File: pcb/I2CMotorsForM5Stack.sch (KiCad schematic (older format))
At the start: 25 parts, among them J1 FFC_connector, J2 2x15socket, J3 Conn_01x06, J4 Conn_01x06, U1 TB6612FNG, U2 ATmega328PB-MU

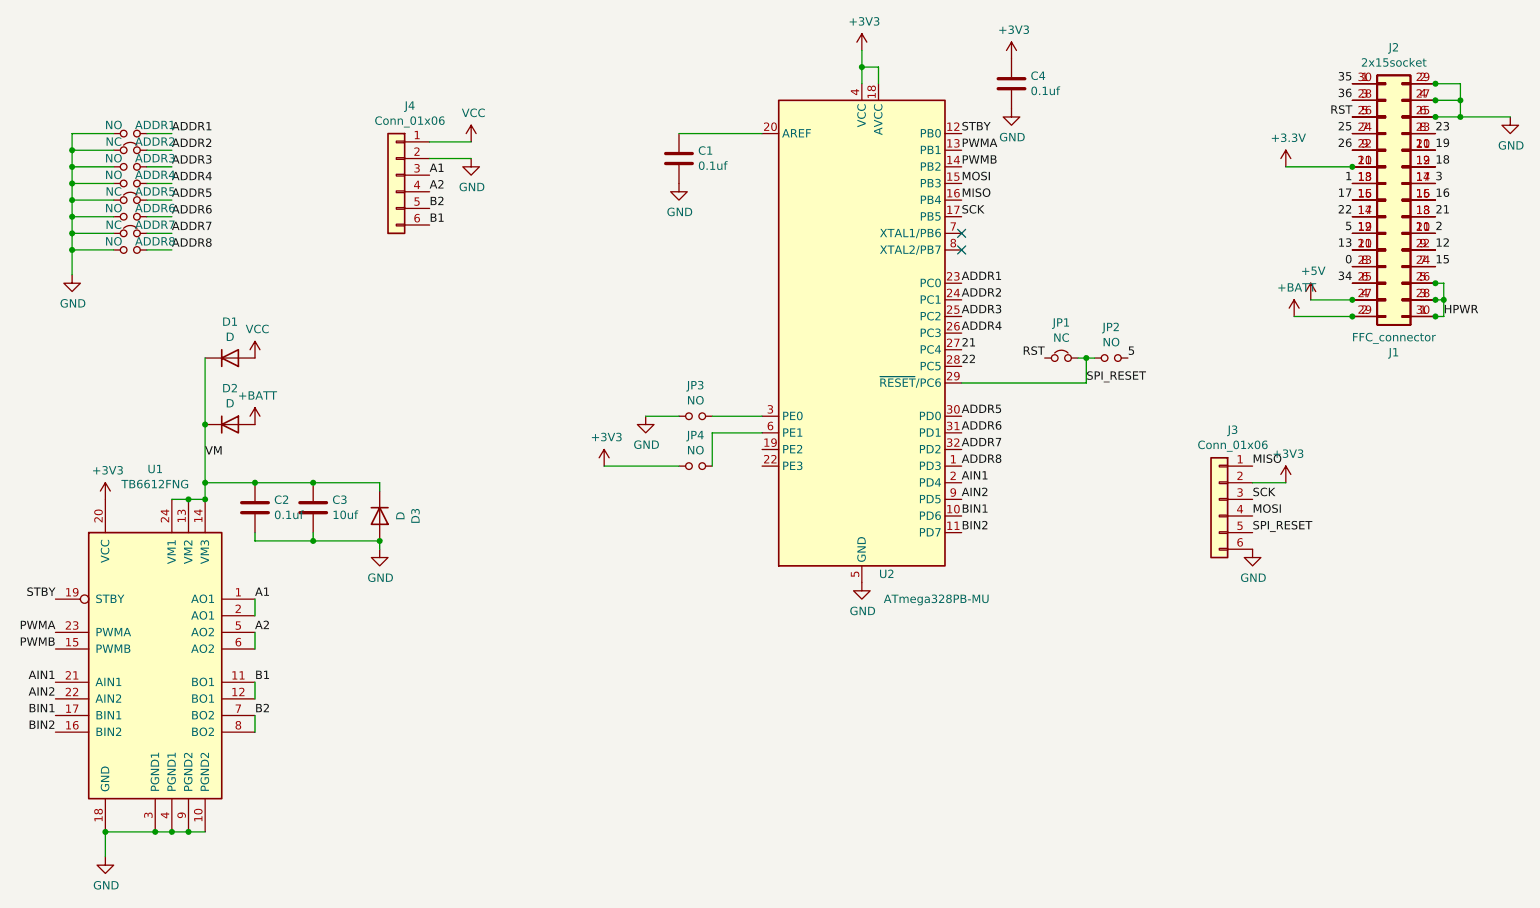
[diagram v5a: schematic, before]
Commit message: Change start number for address pad
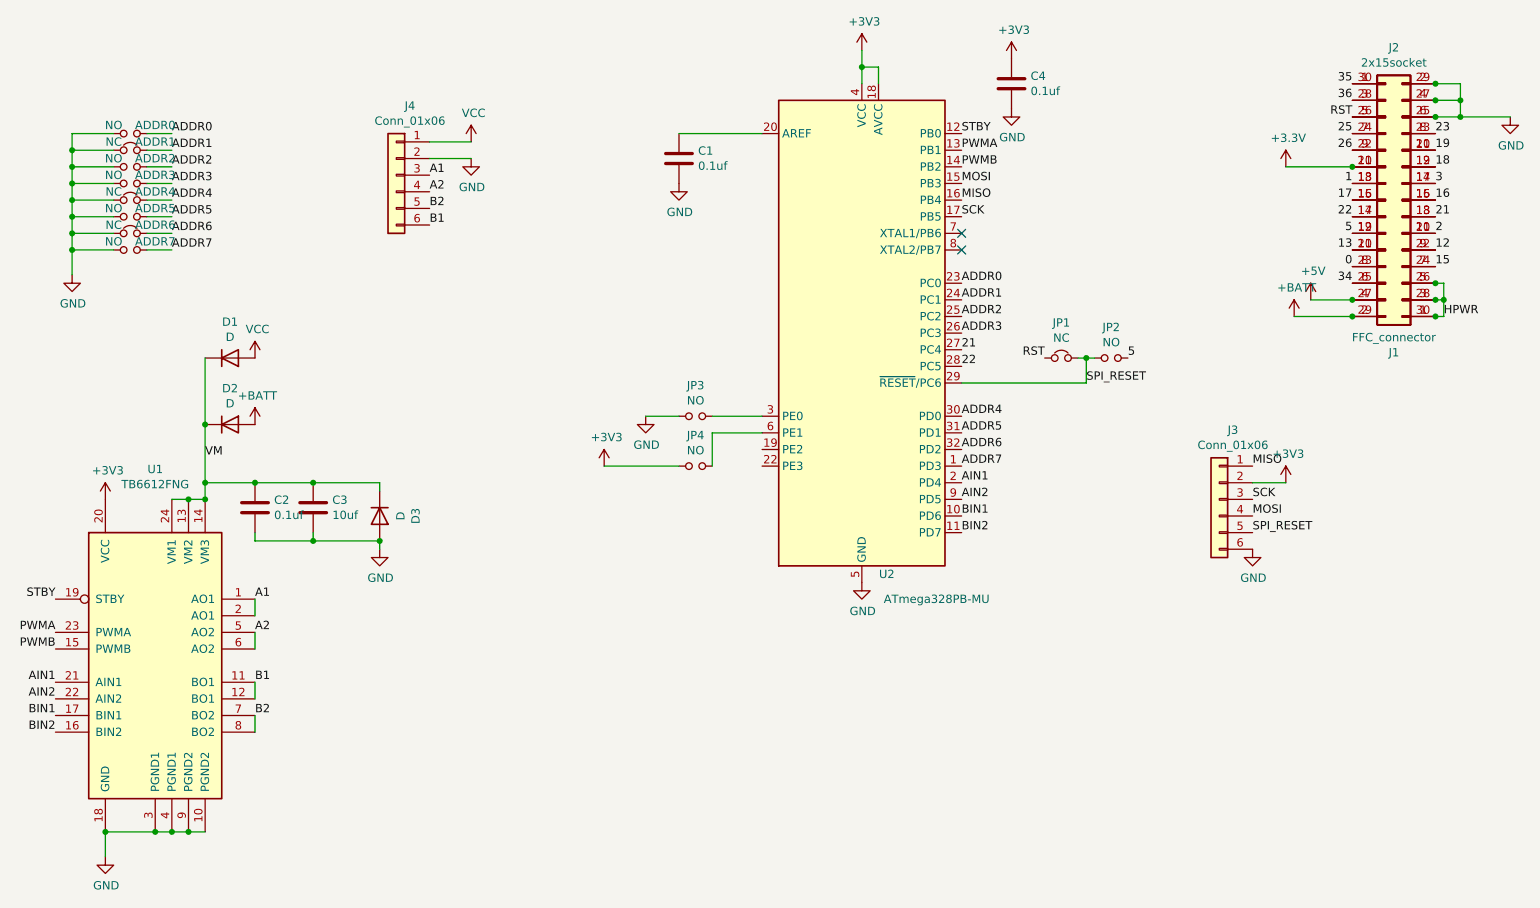
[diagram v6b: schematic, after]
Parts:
- renumbered ADDR1 to ADDR0, ADDR2 to ADDR1, ADDR3 to ADDR2, ADDR4 to ADDR3, ADDR5 to ADDR4, ADDR6 to ADDR5, ADDR7 to ADDR6, ADDR8 to ADDR7
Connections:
- net ADDR8 is gone; now on net ADDR7: ADDR7.2, U2.1 (PD3)
- net ADDR1: now also ADDR1.2, U2.24 (PC1); no longer ADDR0.2, U2.23 (PC0)
- net ADDR2: now also ADDR2.2, U2.25 (PC2); no longer ADDR1.2, U2.24 (PC1)
- net ADDR3: now also ADDR3.2, U2.26 (PC3); no longer ADDR2.2, U2.25 (PC2)
- net ADDR4: now also ADDR4.2, U2.30 (PD0); no longer ADDR3.2, U2.26 (PC3)
- net ADDR5: now also ADDR5.2, U2.31 (PD1); no longer ADDR4.2, U2.30 (PD0)
- net ADDR6: now also ADDR6.2, U2.32 (PD2); no longer ADDR5.2, U2.31 (PD1)
- net ADDR7: no longer ADDR6.2, U2.32 (PD2)
- new net ADDR0: ADDR0.2, U2.23 (PC0)
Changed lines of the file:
@@
 STBY
 Text Label 7350 2900 0    50   ~ 0
-ADDR2
+ADDR1
 $Comp
 L power:GND #PWR0117
@@
 $EndComp
 Text Label 7350 3000 0    50   ~ 0
+ADDR2
+Text Label 7350 3100 0    50   ~ 0
 ADDR3
-Text Label 7350 3100 0    50   ~ 0
+Text Label 7350 3600 0    50   ~ 0
 ADDR4
-Text Label 7350 3600 0    50   ~ 0
+Text Label 7350 3700 0    50   ~ 0
 ADDR5
-Text Label 7350 3700 0    50   ~ 0
+Text Label 7350 3800 0    50   ~ 0
 ADDR6
-Text Label 7350 3800 0    50   ~ 0
+Text Label 7350 3900 0    50   ~ 0
 ADDR7
-Text Label 7350 3900 0    50   ~ 0
-ADDR8
 Text Label 7350 2800 0    50   ~ 0
+ADDR0
+Text Label 2600 1900 0    50   ~ 0
+ADDR0
+Text Label 2600 2000 0    50   ~ 0
 ADDR1
-Text Label 2600 1900 0    50   ~ 0
-ADDR1
-Text Label 2600 2000 0    50   ~ 0
+Text Label 2600 2100 0    50   ~ 0
 ADDR2
-Text Label 2600 2100 0    50   ~ 0
+Text Label 2600 2200 0    50   ~ 0
 ADDR3
-Text Label 2600 2200 0    50   ~ 0
+Text Label 2600 2300 0    50   ~ 0
 ADDR4
-Text Label 2600 2300 0    50   ~ 0
+Text Label 2600 2400 0    50   ~ 0
 ADDR5
-Text Label 2600 2400 0    50   ~ 0
+Text Label 2600 2500 0    50   ~ 0
 ADDR6
-Text Label 2600 2500 0    50   ~ 0
+Text Label 2600 2600 0    50   ~ 0
 ADDR7
-Text Label 2600 2600 0    50   ~ 0
-ADDR8
 $Comp
 L power:+BATT #PWR0107
@@
 $EndComp
 $Comp
-L Device:Jumper_NC_Small ADDR2
+L Device:Jumper_NC_Small ADDR1
 U 1 1 5E84FB49
 P 2350 2000
-F 0 "ADDR2" H 2500 2050 50  0000 C CNN
+F 0 "ADDR1" H 2500 2050 50  0000 C CNN
 F 1 "NC" H 2250 2050 50  0000 C CNN
 F 2 "Jumper:SolderJumper-2_P1.3mm_Bridged_RoundedPad1.0x1.5mm" H 2350 2000 50  0001 C CNN
@@
 $EndComp
 $Comp
-L Device:Jumper_NO_Small ADDR1
+L Device:Jumper_NO_Small ADDR0
 U 1 1 5E8501F7
 P 2350 1900
-F 0 "ADDR1" H 2500 1950 50  0000 C CNN
+F 0 "ADDR0" H 2500 1950 50  0000 C CNN
 F 1 "NO" H 2250 1950 50  0000 C CNN
 F 2 "Jumper:SolderJumper-2_P1.3mm_Open_RoundedPad1.0x1.5mm" H 2350 1900 50  0001 C CNN
@@
 	2000 1900 2000 2000
 $Comp
-L Device:Jumper_NO_Small ADDR3
+L Device:Jumper_NO_Small ADDR2
 U 1 1 5E855E5F
 P 2350 2100
-F 0 "ADDR3" H 2500 2150 50  0000 C CNN
+F 0 "ADDR2" H 2500 2150 50  0000 C CNN
 F 1 "NO" H 2250 2150 50  0000 C CNN
 F 2 "Jumper:SolderJumper-2_P1.3mm_Open_RoundedPad1.0x1.5mm" H 2350 2100 50  0001 C CNN
@@
 $EndComp
 $Comp
-L Device:Jumper_NO_Small ADDR4
+L Device:Jumper_NO_Small ADDR3
 U 1 1 5E855FAF
 P 2350 2200
-F 0 "ADDR4" H 2500 2250 50  0000 C CNN
+F 0 "ADDR3" H 2500 2250 50  0000 C CNN
 F 1 "NO" H 2250 2250 50  0000 C CNN
 F 2 "Jumper:SolderJumper-2_P1.3mm_Open_RoundedPad1.0x1.5mm" H 2350 2200 50  0001 C CNN
@@
 $EndComp
 $Comp
-L Device:Jumper_NC_Small ADDR5
+L Device:Jumper_NC_Small ADDR4
 U 1 1 5E8560B1
 P 2350 2300
-F 0 "ADDR5" H 2500 2350 50  0000 C CNN
+F 0 "ADDR4" H 2500 2350 50  0000 C CNN
 F 1 "NC" H 2250 2350 50  0000 C CNN
 F 2 "Jumper:SolderJumper-2_P1.3mm_Bridged_RoundedPad1.0x1.5mm" H 2350 2300 50  0001 C CNN
@@
 $EndComp
 $Comp
-L Device:Jumper_NO_Small ADDR6
+L Device:Jumper_NO_Small ADDR5
 U 1 1 5E856295
 P 2350 2400
-F 0 "ADDR6" H 2500 2450 50  0000 C CNN
+F 0 "ADDR5" H 2500 2450 50  0000 C CNN
 F 1 "NO" H 2250 2450 50  0000 C CNN
 F 2 "Jumper:SolderJumper-2_P1.3mm_Open_RoundedPad1.0x1.5mm" H 2350 2400 50  0001 C CNN
@@
 $EndComp
 $Comp
-L Device:Jumper_NC_Small ADDR7
+L Device:Jumper_NC_Small ADDR6
 U 1 1 5E856411
 P 2350 2500
-F 0 "ADDR7" H 2500 2550 50  0000 C CNN
+F 0 "ADDR6" H 2500 2550 50  0000 C CNN
 F 1 "NC" H 2250 2550 50  0000 C CNN
 F 2 "Jumper:SolderJumper-2_P1.3mm_Bridged_RoundedPad1.0x1.5mm" H 2350 2500 50  0001 C CNN
@@
 $EndComp
 $Comp
-L Device:Jumper_NO_Small ADDR8
+L Device:Jumper_NO_Small ADDR7
 U 1 1 5E8565AF
 P 2350 2600
-F 0 "ADDR8" H 2500 2650 50  0000 C CNN
+F 0 "ADDR7" H 2500 2650 50  0000 C CNN
 F 1 "NO" H 2250 2650 50  0000 C CNN
 F 2 "Jumper:SolderJumper-2_P1.3mm_Open_RoundedPad1.0x1.5mm" H 2350 2600 50  0001 C CNN

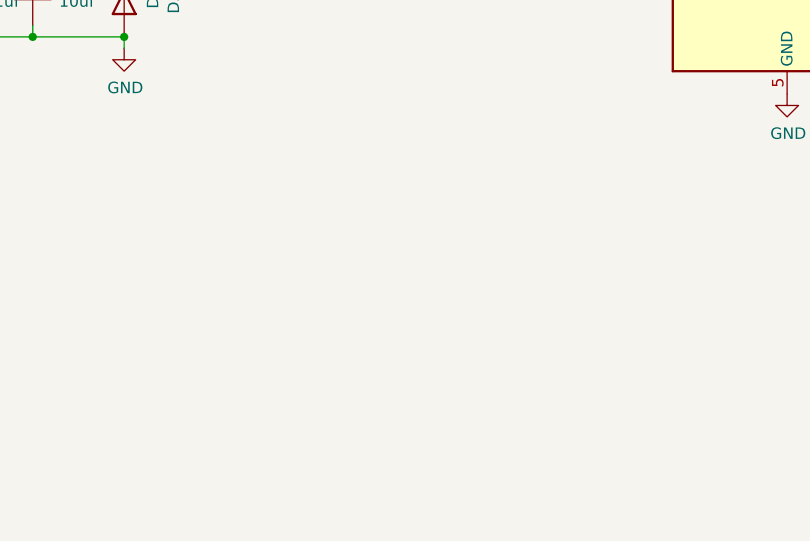
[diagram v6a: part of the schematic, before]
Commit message: Add connector to support power lines
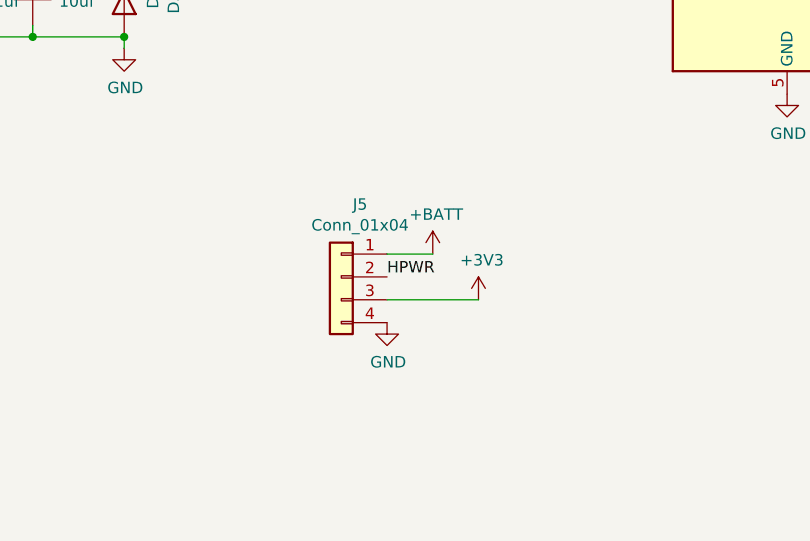
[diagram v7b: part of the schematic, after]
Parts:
- added J5: Conn_01x04, Connector:NS-Tech_Grove_1x04_P2mm_Vertical, symbol Connector_Generic:Conn_01x04
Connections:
- net +3V3: now also J5.3 (Pin_3)
- net +BATT: now also J5.1 (Pin_1)
- net GND: now also J5.4 (Pin_4)
- net HPWR: now also J5.2 (Pin_2)
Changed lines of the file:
@@
 Wire Wire Line
 	2450 2600 2600 2600
+$Comp
+L Connector_Generic:Conn_01x04 J5
+U 1 1 5EAF40C4
+P 4800 5400
+F 0 "J5" H 4718 5717 50  0000 C CNN
+F 1 "Conn_01x04" H 4718 5626 50  0000 C CNN
+F 2 "Connector:NS-Tech_Grove_1x04_P2mm_Vertical" H 4800 5400 50  0001 C CNN
+F 3 "~" H 4800 5400 50  0001 C CNN
+	1    4800 5400
+	-1   0    0    -1
+$EndComp
+$Comp
+L power:GND #PWR0116
+U 1 1 5EAF8315
+P 5000 5600
+F 0 "#PWR0116" H 5000 5350 50  0001 C CNN
+F 1 "GND" H 5005 5427 50  0000 C CNN
+F 2 "" H 5000 5600 50  0001 C CNN
+F 3 "" H 5000 5600 50  0001 C CNN
+	1    5000 5600
+	1    0    0    -1
+$EndComp
+Text Label 5000 5400 0    50   ~ 0
+HPWR
+Wire Wire Line
+	5200 5300 5000 5300
+$Comp
+L power:+3V3 #PWR0123
+U 1 1 5EAFA395
+P 5400 5500
+F 0 "#PWR0123" H 5400 5350 50  0001 C CNN
+F 1 "+3V3" H 5415 5673 50  0000 C CNN
+F 2 "" H 5400 5500 50  0001 C CNN
+F 3 "" H 5400 5500 50  0001 C CNN
+	1    5400 5500
+	1    0    0    -1
+$EndComp
+Wire Wire Line
+	5000 5500 5400 5500
+$Comp
+L power:+BATT #PWR0124
+U 1 1 5EAFD8AA
+P 5200 5300
+F 0 "#PWR0124" H 5200 5150 50  0001 C CNN
+F 1 "+BATT" H 5215 5473 50  0000 C CNN
+F 2 "" H 5200 5300 50  0001 C CNN
+F 3 "" H 5200 5300 50  0001 C CNN
+	1    5200 5300
+	1    0    0    -1
+$EndComp
 $EndSCHEMATC
